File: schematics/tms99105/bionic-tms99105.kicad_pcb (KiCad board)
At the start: 2 copper layers, 48.3 x 71.1 mm, 10 parts, among them J1 Bionic-P135, J2 Bionic-P245, U1 TMS99105, U2 74HCT126, U3 11AA010-I/TO

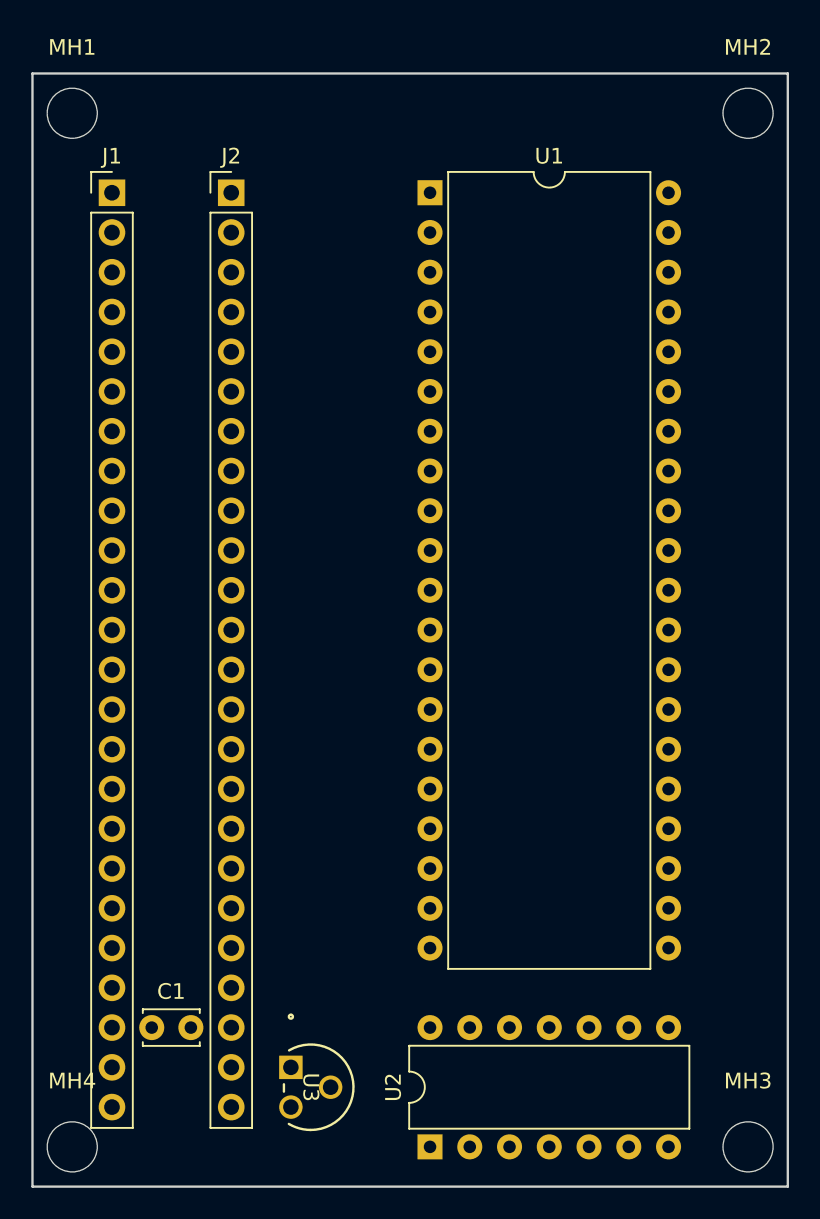
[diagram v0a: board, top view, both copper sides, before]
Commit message: [TMS99105] Update schematics
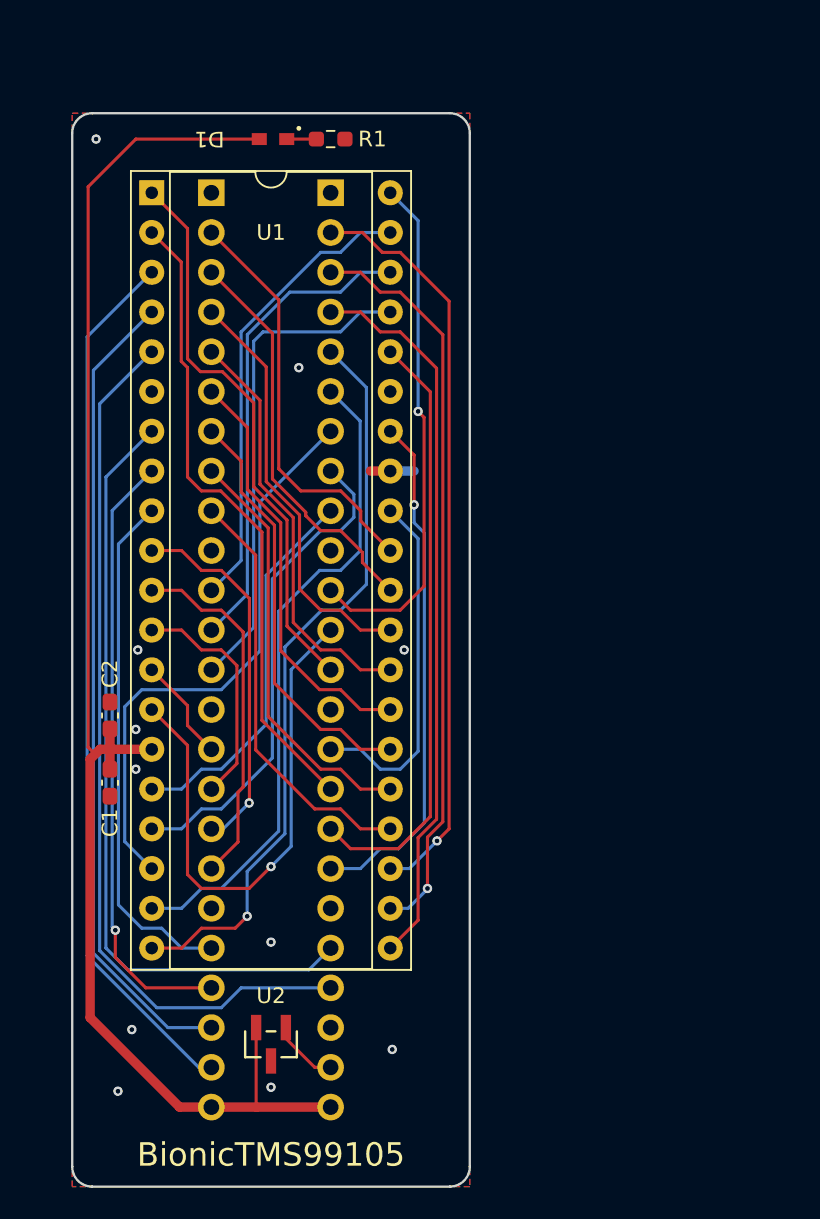
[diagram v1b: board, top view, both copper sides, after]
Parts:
- removed MH1, MH2, MH3, MH4: MountingHole_3.2mm_M3, MountingHole:MountingHole_3.2mm_M3
- removed U3: 11AA010-I/TO, microchip:TO-92_MC_MCH
- added C2: 22U, Capacitor_SMD:C_0603_1608Metric_Pad1.08x0.95mm_HandSolder, F.Cu at (103.4, 108.5)
- added D1: CSL1901UW1, 0-LocalLibrary:LED_CSL1901UW1_ROM-M, F.Cu at (113.8, 71.7)
- added R1: 1.6k, Resistor_SMD:R_0603_1608Metric_Pad0.98x0.95mm_HandSolder, F.Cu at (117.5, 71.7)
- C1: footprint Capacitor_THT:C_Disc_D3.4mm_W2.1mm_P2.50mm -> Capacitor_SMD:C_0603_1608Metric_Pad1.08x0.95mm_HandSolder
- J1: footprint connector:Bionic-P135_Vertical -> 0-LocalLibrary:Bionic-P135_Vertical; moved to B.Cu
- J2: footprint connector:Bionic-P245_Vertical -> 0-LocalLibrary:Bionic-P245_Vertical; moved to B.Cu
- U1: footprint Package_DIP:DIP-40_W15.24mm -> 0-LocalLibrary:DIP-40_W15.24mm_Socket
- U2: value 74HCT126 -> 11AA010-I/TT; footprint Package_DIP:DIP-14_W7.62mm -> 0-LocalLibrary:SOT-23_MC_MCH-M
- moved U1 17.8 mm to (106.1, 75.1)
- moved C1 15.9 mm to (103.4, 112.8), turned to -90 degrees
- moved U2 12.1 mm to (113.7, 129.5), turned to 180 degrees
- moved J2 6.35 mm to (117.5, 75.1), turned to 180 degrees
- moved J1 6.35 mm to (109.9, 75.1), turned to 180 degrees
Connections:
- J1 pad 10: unconnected-(J1-E0-Pad10) -> (no net)
- J1 pad 14: unconnected-(J1-P33-Pad14) -> (no net)
- J1 pad 17: /P36 -> /P37
- J1 pad 18: /P37 -> /P36
- J1 pad 19: unconnected-(J1-15V-Pad19) -> (no net)
- J2 pad 26: Net-(J2-P57) -> unconnected-(U2-SCIO-Pad1)
- J2 pad 27: unconnected-(J2-P56-Pad27) -> (no net)
- J2 pad 28: unconnected-(J2-P55-Pad28) -> /P55
- J2 pad 30: unconnected-(J2-15V-Pad30) -> (no net)
- J2 pad 35: /P43 -> (no net)
- J2 pad 39: unconnected-(J2-E1-Pad39) -> (no net)
- U1 pad 1: /P51 -> /P42
- U1 pad 14: /P45 -> /P41
- U1 pad 2: /P50 -> /P45
- U1 pad 36: Net-(U1-CLKIN) -> /P46
- U1 pad 37: /P30 -> /P32
- U1 pad 39: /P32 -> /P30
- U1 pad 4: /P41 -> /P52
- U1 pad 40: /P54 -> /P40
- U1 pad 5: /P40 -> /P55
- U1 pad 7: /P52 -> /P54
- U1 pad 8: /P42 -> /P51
- U1 pad 9: /P43 -> /P50
- U2 pad 1: VCC -> unconnected-(U2-SCIO-Pad1)
- U2 pad 2: /P46 -> VCC
- U2 pad 3: Net-(U1-CLKIN) -> GND
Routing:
- net VCC: track 0.00 -> 94.7 mm
- net /P55: track 0.00 -> 56.4 mm
- net /P53: track 0.00 -> 56.3 mm
- net /P52: track 0.00 -> 52.0 mm
- net /P54: track 0.00 -> 49.7 mm
- net /P20: track 0.00 -> 47.9 mm, vias 0 -> 1
- net /P23: track 0.00 -> 47.8 mm, vias 0 -> 1
- net /P21: track 0.00 -> 47.5 mm, vias 0 -> 1
- net /P22: track 0.00 -> 46.5 mm
- net /P24: track 0.00 -> 42.0 mm
- net /P45: track 0.00 -> 41.0 mm
- net /P51: track 0.00 -> 39.1 mm, vias 0 -> 1
- net /P46: track 0.00 -> 38.5 mm
- net /P25: track 0.00 -> 37.1 mm
- net /P42: track 0.00 -> 36.0 mm
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- added copper zone on B.Cu, net GND
- added copper zone on F.Cu, net GND
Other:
- board size 48.3 x 71.1 mm -> 25.4 x 68.6 mm
- board text added: "BionicTMS99105"
- board text added: "JLCJLCJLCJLC"
- board text added: "Rev. 2"

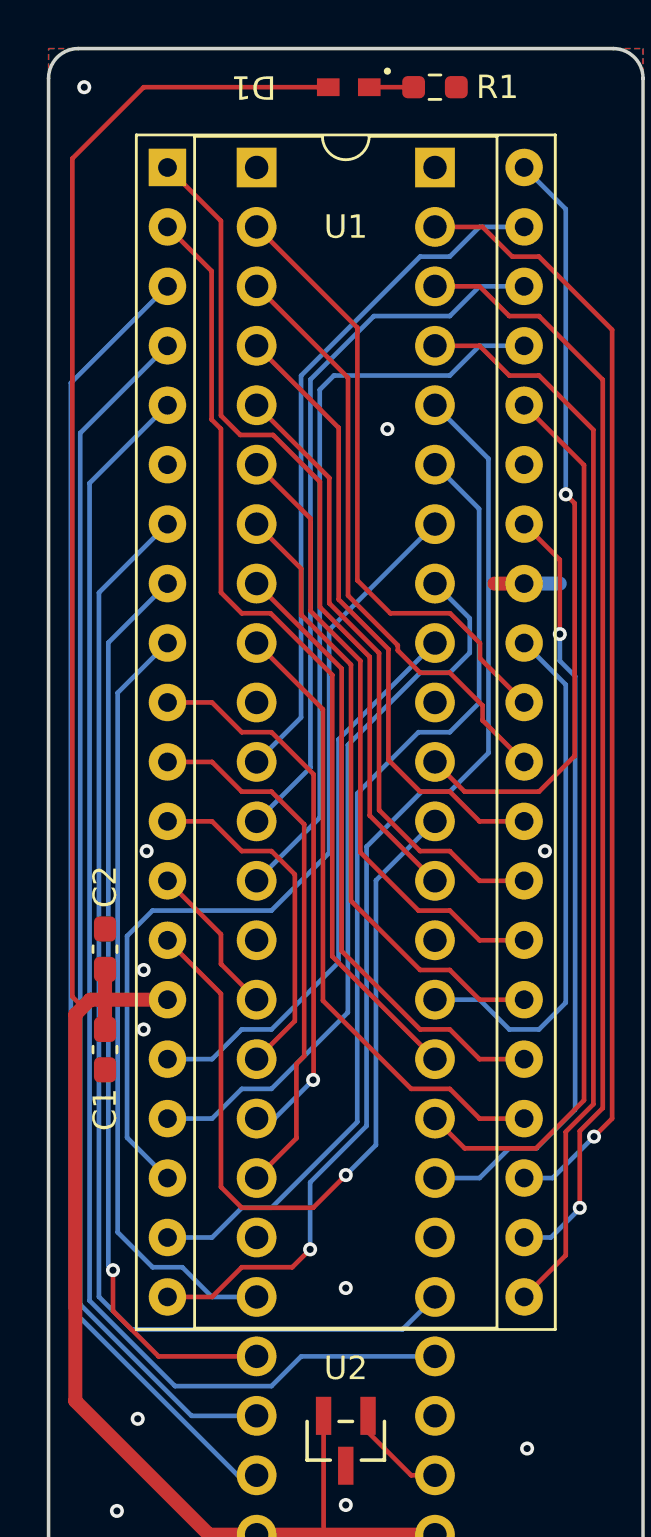
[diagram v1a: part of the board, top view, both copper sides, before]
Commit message: [TMS99105] Cleanup schematics
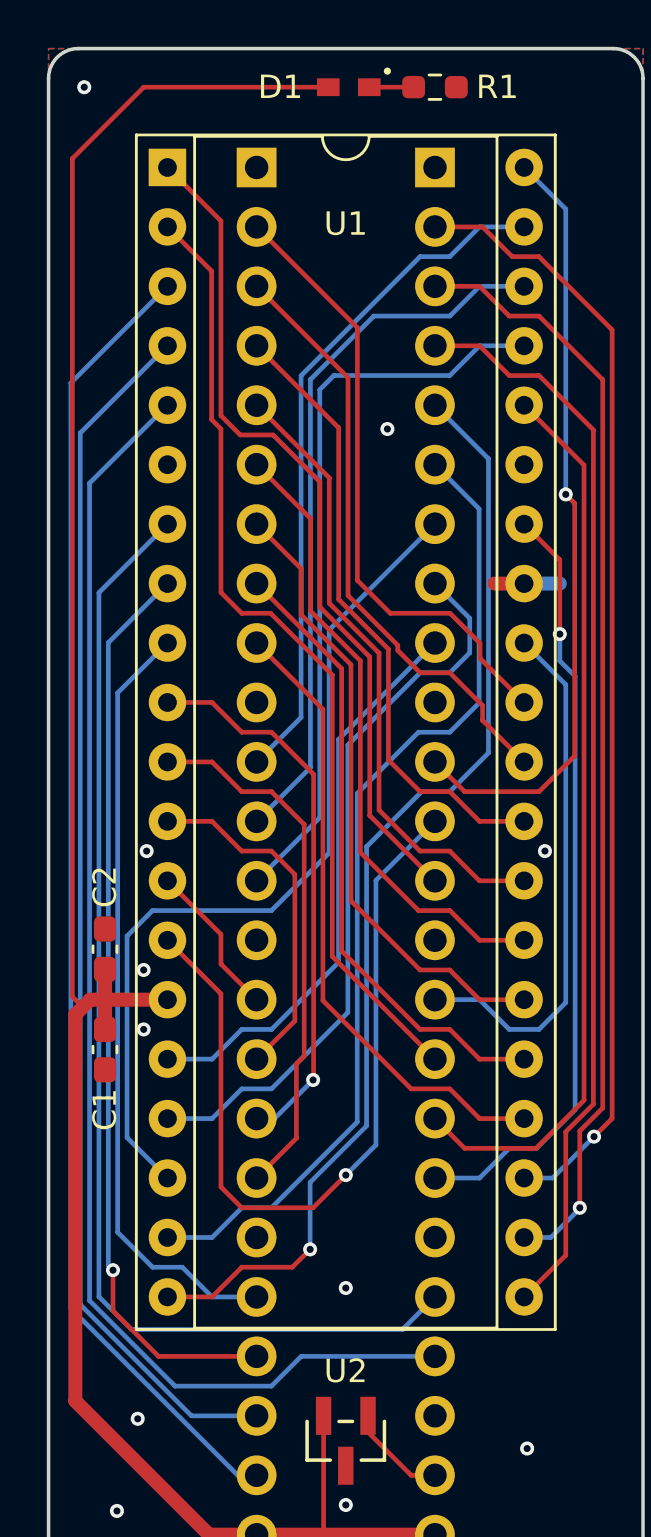
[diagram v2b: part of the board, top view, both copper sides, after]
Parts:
- D1: footprint 0-LocalLibrary:LED_CSL1901UW1_ROM-M -> rhom:LED_CSL1901UW1_ROM-M
- J1: footprint 0-LocalLibrary:Bionic-P135_Vertical -> bionic:Bionic-P135_Vertical
- J2: footprint 0-LocalLibrary:Bionic-P245_Vertical -> bionic:Bionic-P245_Vertical
- U1: footprint 0-LocalLibrary:DIP-40_W15.24mm_Socket -> bionic:DIP-40_W15.24mm_Socket
- U2: footprint 0-LocalLibrary:SOT-23_MC_MCH-M -> microchip:SOT-23_MC_MCH-M
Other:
- rule pad_to_mask_clearance: 0.051 -> 0
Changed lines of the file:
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@@
 			(dielectric_constraints no)
 		)
-		(pad_to_mask_clearance 0.051)
-		(solder_mask_min_width 0.25)
+		(pad_to_mask_clearance 0)
 		(allow_soldermask_bridges_in_footprints no)
 		(aux_axis_origin 101 70)
@@
 		)
 	)
-	(footprint "0-LocalLibrary:LED_CSL1901UW1_ROM-M"
+	(footprint "rhom:LED_CSL1901UW1_ROM-M"
 		(layer "F.Cu")
 		(at 113.827 71.651 180)
@@
 		(tags "CSL1901UW1 ")
 		(property "Reference" "D1"
-			(at 4.064 0 180)
+			(at 2.921 0 0)
 			(unlocked yes)
 			(layer "F.SilkS")
@@
 			)
 		)
-		(property "Footprint" "0-LocalLibrary:LED_CSL1901UW1_ROM-M"
-			(at 0 0 360)
+		(property "Footprint" "rhom:LED_CSL1901UW1_ROM-M"
+			(at 0 0 180)
 			(layer "F.Fab")
 			(hide yes)
@@
 		)
 		(property "Datasheet" "https://fscdn.rohm.com/en/products/databook/datasheet/opto/led/chip_mono/csl1901uw1-e.pdf"
-			(at 0 0 360)
+			(at 0 0 180)
 			(layer "F.Fab")
 			(hide yes)
@@
 		)
 		(property "Description" "Red LED (Low Current Emission, SMD)"
-			(at 0 0 360)
+			(at 0 0 180)
 			(layer "F.Fab")
 			(hide yes)
@@
 			)
 		)
-		(model "${KIPRJMOD}/0-LocalLibrary/LED_CSL1901UW1_ROM.step"
+		(model "${KIPRJMOD}/rhom.pretty/LED_CSL1901UW1_ROM.step"
 			(offset
 				(xyz 0 0 0)
@@
 		)
 	)
-	(footprint "0-LocalLibrary:DIP-40_W15.24mm_Socket"
+	(footprint "bionic:DIP-40_W15.24mm_Socket"
 		(locked yes)
 		(layer "F.Cu")
@@
 		(tags "THT DIP DIL PDIP 2.54mm 15.24mm 600mil Socket")
 		(property "Reference" "U1"
-			(at 7.62 2.54 0)
+			(at 7.62 2.413 0)
 			(layer "F.SilkS")
 			(effects
@@
 			)
 		)
-		(property "Footprint" "0-LocalLibrary:DIP-40_W15.24mm_Socket"
+		(property "Footprint" "bionic:DIP-40_W15.24mm_Socket"
 			(at 0 0 0)
 			(layer "F.Fab")
@@
 		)
 	)
-	(footprint "0-LocalLibrary:SOT-23_MC_MCH-M"
+	(footprint "microchip:SOT-23_MC_MCH-M"
 		(layer "F.Cu")
 		(at 113.7 129.486 180)
 		(descr "Microchip 11AAxxx-I/TT UNI/O 1Kbit Serial EEPROM")
 		(property "Reference" "U2"
-			(at 0 3.098 0)
+			(at 0 2.971 0)
 			(unlocked yes)
 			(layer "F.SilkS")
@@
 			)
 		)
-		(property "Footprint" "0-LocalLibrary:SOT-23_MC_MCH-M"
-			(at 0 0 0)
+		(property "Footprint" "microchip:SOT-23_MC_MCH-M"
+			(at 0 0 180)
 			(layer "F.Fab")
 			(hide yes)
@@
 		)
 		(property "Datasheet" "11AA010-I/TO"
-			(at 0 0 0)
+			(at 0 0 180)
 			(layer "F.Fab")
 			(hide yes)
@@
 		)
 		(property "Description" "UNI/O Serial EEPROM (1Kbit)"
-			(at 0 0 0)
+			(at 0 0 180)
 			(layer "F.Fab")
 			(hide yes)
@@
 			(pintype "power_in")
 		)
-		(model "${KIPRJMOD}/0-LocalLibrary/SOT-23_MC_MCH.step"
+		(model "${KIPRJMOD}/microchip.pretty/SOT-23_MC_MCH.step"
 			(offset
 				(xyz 0 0 0)
@@
 		)
 	)
-	(footprint "0-LocalLibrary:Bionic-P135_Vertical"
+	(footprint "bionic:Bionic-P135_Vertical"
 		(locked yes)
 		(layer "B.Cu")
@@
 			)
 		)
-		(property "Footprint" "0-LocalLibrary:Bionic-P135_Vertical"
+		(property "Footprint" "bionic:Bionic-P135_Vertical"
 			(at 0 0 0)
 			(layer "B.Fab")
@@
 		)
 	)
-	(footprint "0-LocalLibrary:Bionic-P245_Vertical"
+	(footprint "bionic:Bionic-P245_Vertical"
 		(locked yes)
 		(layer "B.Cu")
@@
 			)
 		)
-		(property "Footprint" "0-LocalLibrary:Bionic-P245_Vertical"
+		(property "Footprint" "bionic:Bionic-P245_Vertical"
 			(at 0 0 0)
 			(layer "B.Fab")

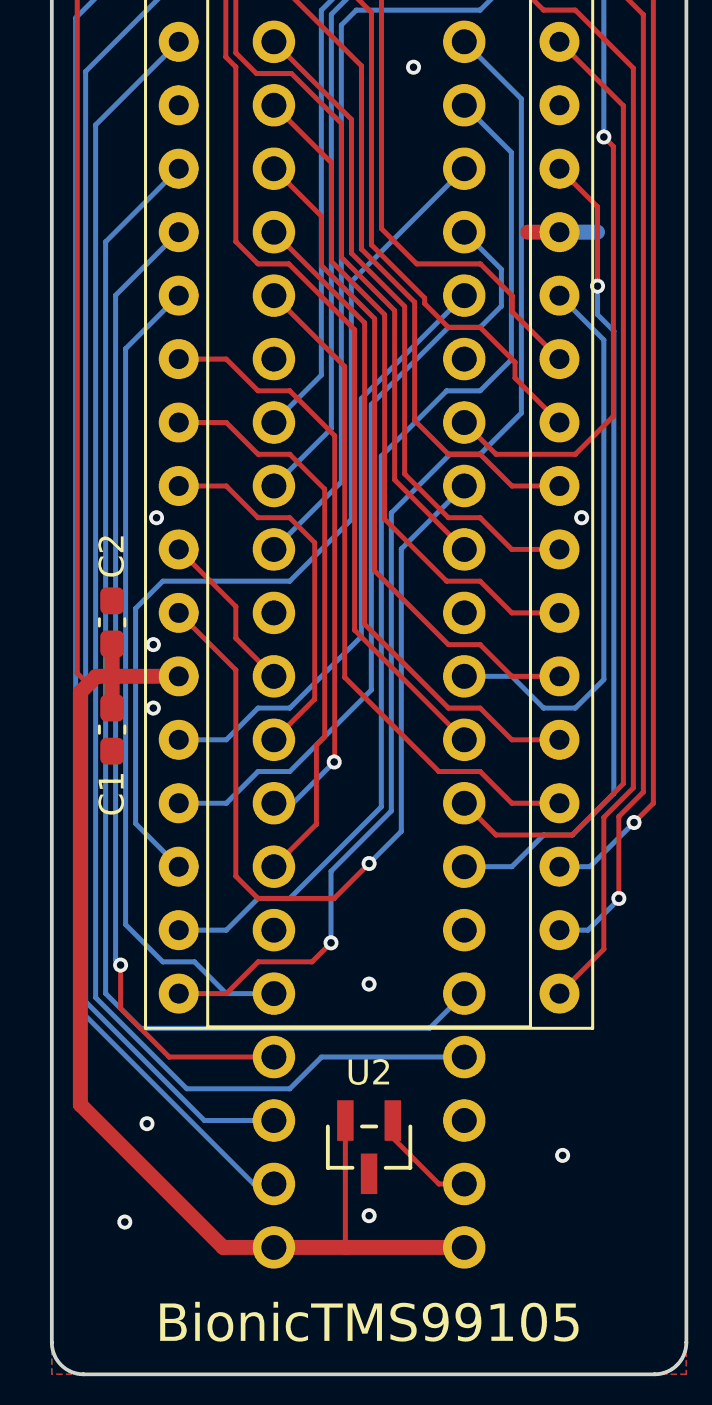
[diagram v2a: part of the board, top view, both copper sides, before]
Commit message: [TMS99105] Update schematics
Remove unused pins from bionic connector
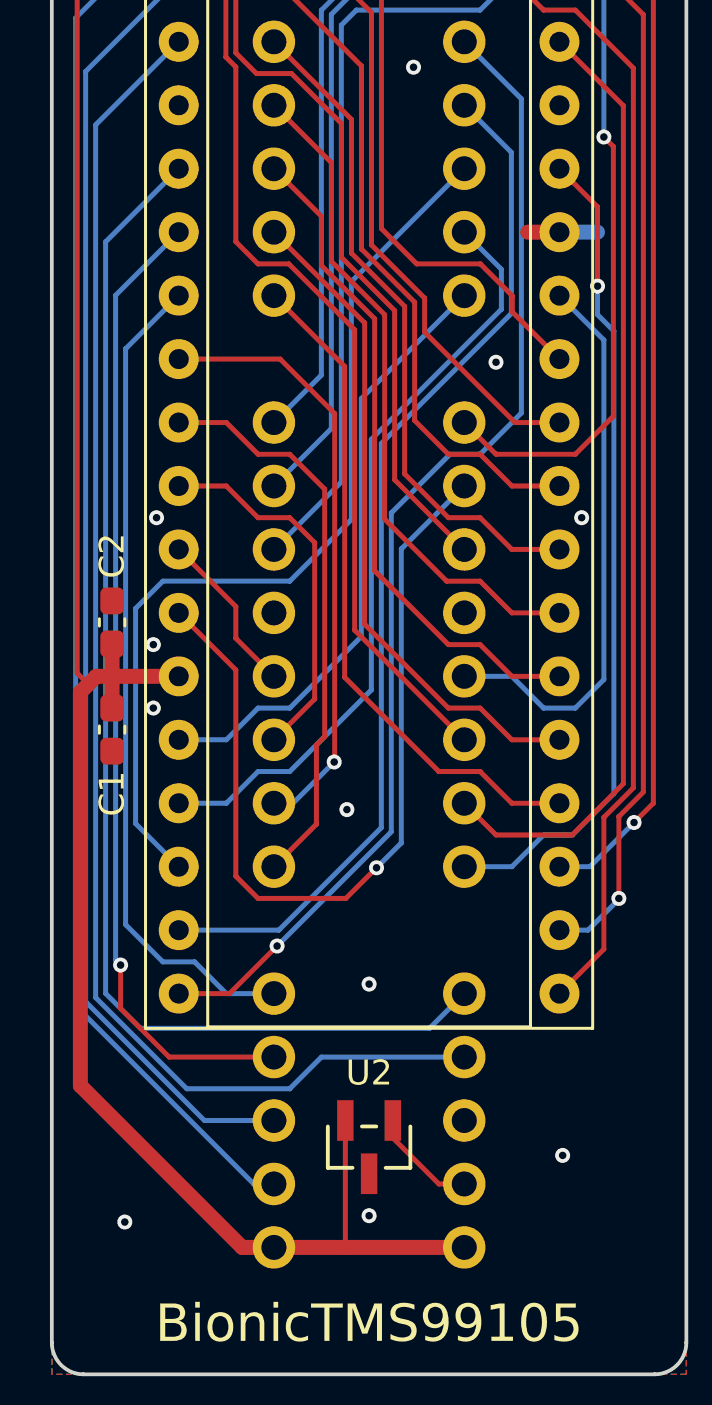
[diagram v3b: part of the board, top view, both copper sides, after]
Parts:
- J1: footprint bionic:Bionic-P135_Vertical -> bionic:Bionic-P135_THT
- J2: footprint bionic:Bionic-P245_Vertical -> bionic:Bionic-P245_THT
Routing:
- net /P23: track 47.8 -> 46.6 mm
- net /P26: track 31.4 -> 30.7 mm
- net /P37: track 23.7 -> 24.2 mm
- net GND: vias 11 -> 12
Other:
- board text added: "Rev. 3"
- board text removed: "Rev. 2"
